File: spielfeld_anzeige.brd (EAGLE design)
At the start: 100 x 60 mm, 19 parts, among them IC1 UDN2981A, IC2 UDN2981A, IC3 74HC595N, IC4 74HC595N, IC5 74HC595N

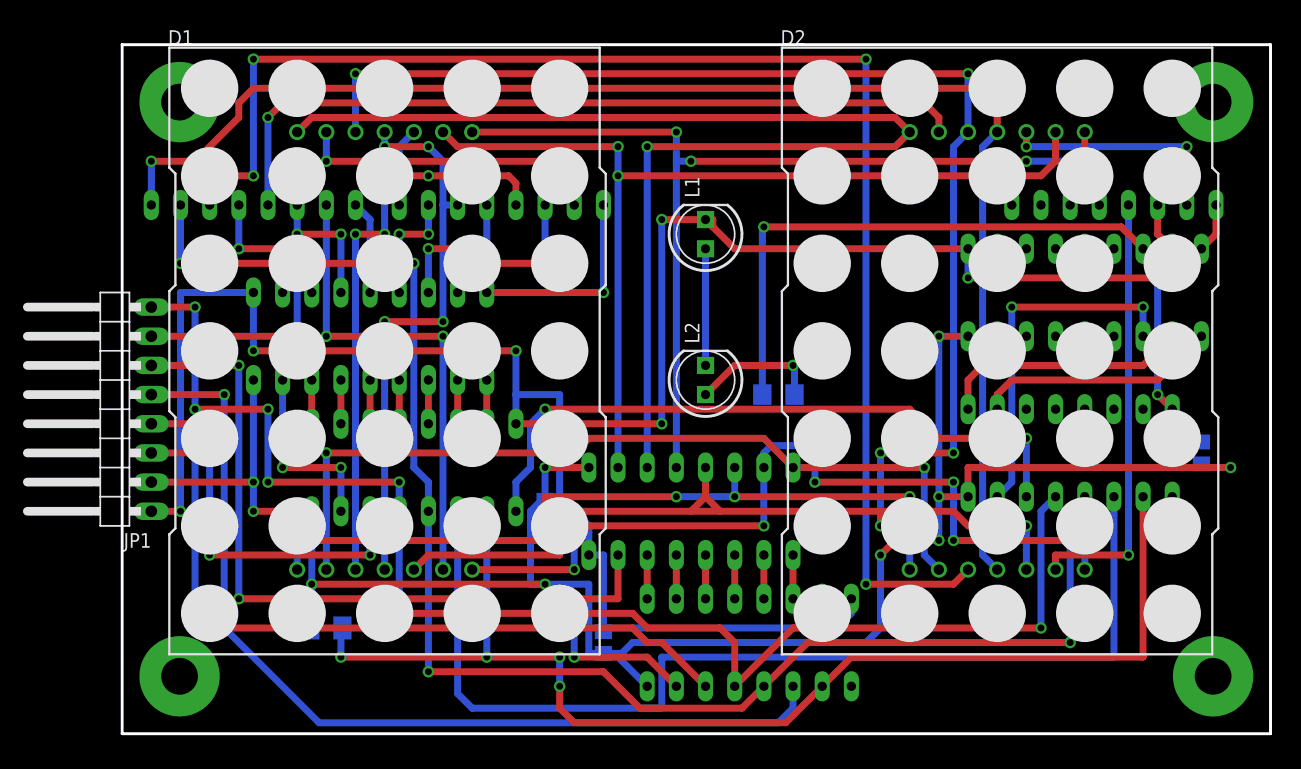
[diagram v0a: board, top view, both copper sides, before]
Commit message: Revision due to Pete and Leander on 30.04.2018
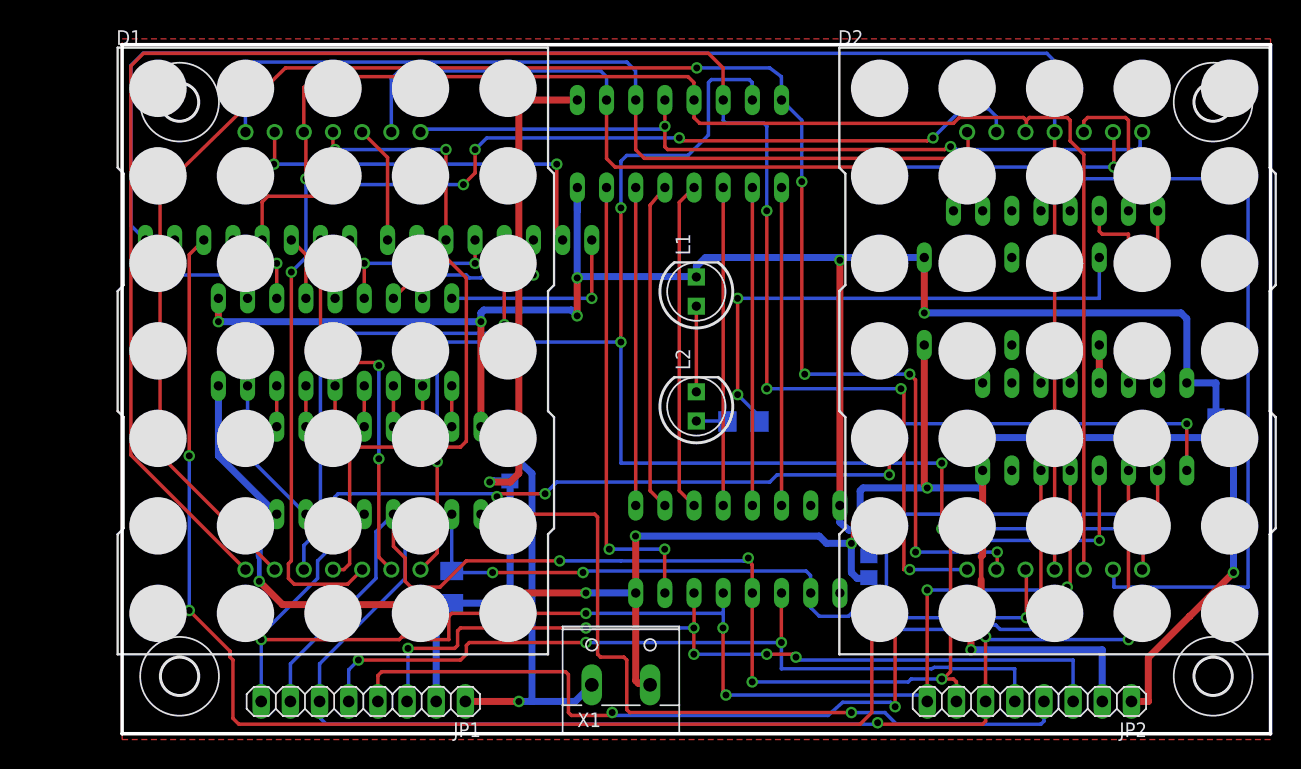
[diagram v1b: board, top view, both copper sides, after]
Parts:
- added H1, H2, H3, H4: MOUNT-HOLE3.2, holes:3,2
- added JP2: OUT, pinhead:1X08
- added X1: (no value), con-wago-508:W237-132
- JP1: value 8 Pin -> IN; device pinhead:1X08/90 -> pinhead:1X08
- RN1, RN2, RN3: value 180 -> 120
- moved JP1 33.8 mm to (21.0, 22.8), turned to 180 degrees
- moved ICL1 32.0 mm to (48.5, 71.4)
- moved C1 24.0 mm to (65.0, 34.5)
- moved R3 11.5 mm to (28.7, 32.8), turned to 270 degrees
- moved IC3 8.19 mm to (53.6, 36.1)
- moved RN3 5.11 mm to (81.3, 65.5)
- moved L1 5.06 mm to (50.0, 58.5)
- moved D2 5.00 mm to (81.2, 53.3)
- moved C2 4.72 mm to (33.8, 43.0), turned to 90 degrees
- moved D1 4.50 mm to (18.4, 53.3)
- moved IC2 3.89 mm to (80.0, 57.7)
- moved R1 3.84 mm to (54.1, 47.2), turned to 180 degrees
- moved RN1 3.21 mm to (32.0, 63.0)
- moved RN2 3.09 mm to (10.9, 63.0)
- moved IC1 3.09 mm to (18.5, 54.1)
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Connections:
- new net COL_SER_OUT: IC4.9, JP2.4
- net !ENABLE!: now also JP2.8
- net +5V: now also JP2.2, X1.2
- net COLON: now also IC5.5; no longer IC5.15
- net COL_SCK: now also JP2.6
- net COL_SER: now also IC5.14; no longer IC4.14
- net D2_C4: now also IC5.7; no longer IC5.2
- net D2_C5: now also IC5.6; no longer IC5.1
- net GND: now also JP2.1, X1.1
- net N$20: now also IC4.14, IC5.9; no longer IC4.9, IC5.14
- net RCK: now also JP2.7
- net ROW_SCK: now also JP2.5
- net ROW_SER: now also JP2.3
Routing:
- net R5_OUT: track 68.6 -> 165.0 mm
- net R7_OUT: track 73.2 -> 156.1 mm, vias 2 -> 6
- net COL_SER_OUT: track 0.00 -> 68.0 mm, vias 0 -> 1
- net R6_OUT: track 73.4 -> 136.1 mm, vias 7 -> 6
- net +5V: track 175.8 -> 236.4 mm
- net COL_SER: track 34.3 -> 85.0 mm, vias 3 -> 4
- net D2_C5_OUT: track 38.1 -> 67.1 mm
- net COLON: track 31.0 -> 3.30 mm, vias 2 -> 0
- net R2_OUT: track 105.7 -> 78.3 mm, vias 1 -> 0
- net N$20: track 58.0 -> 85.2 mm, vias 2 -> 5
- net N$11: track 3.81 -> 28.8 mm
- net N$10: track 3.81 -> 28.7 mm
- net !SCLR!: track 106.5 -> 81.9 mm, vias 4 -> 3
- net COL_SCK: track 139.0 -> 115.1 mm
- net N$9: track 3.81 -> 27.7 mm
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- added copper zone on layer 1, net GND

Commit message: Changed Layout (in Progress)
Updated Eagle-Borad and Schematic
- Reorganize the outputs of the FFs
- Move Colon to FF for Rows
- Change resistors to 0805 and 82 Ohm
- Put all devices in Layout back to 50 mil grid
- startet layout from scratch
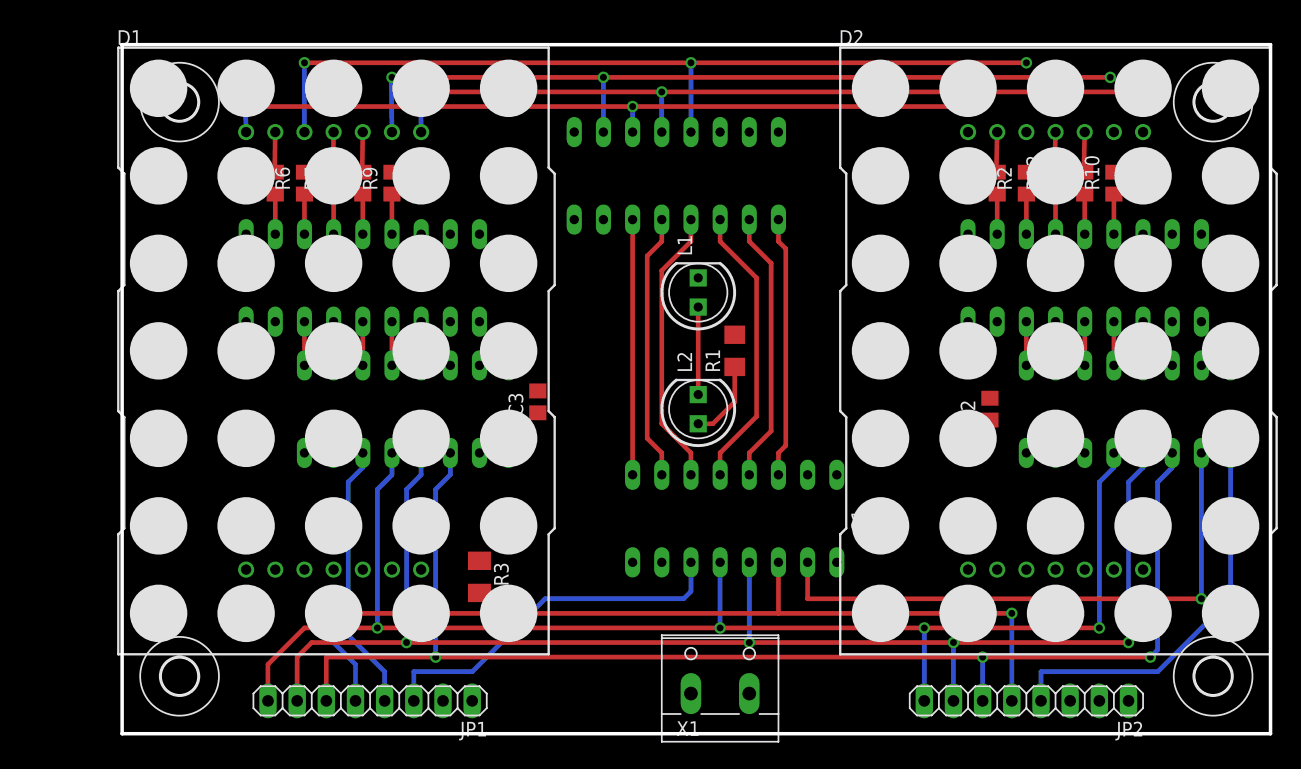
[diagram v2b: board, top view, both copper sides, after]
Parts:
- removed RN1, RN2, RN3: 120, resistor-sil:SIL8
- added R10, R11, R12, R2, R4, R5, R6, R7, R8, R9: 82, rcl:R0805
- moved IC1 65.5 mm to (83.8, 59.7)
- moved IC4 65.5 mm to (87.6, 48.3)
- moved C3 59.1 mm to (36.2, 48.9), flipped to the top
- moved IC2 59.1 mm to (21.0, 59.7)
- moved IC5 59.1 mm to (24.8, 48.3)
- moved C2 42.1 mm to (75.6, 48.3), flipped to the top
- moved X1 8.67 mm to (52.1, 24.1)
- moved R1 6.20 mm to (53.3, 53.3), flipped to the top, turned to 90 degrees
- moved C1 4.31 mm to (66.0, 38.7), flipped to the top
- moved ICL1 2.80 mm to (48.3, 68.6)
- moved IC3 2.68 mm to (53.3, 38.7)
- moved R3 2.57 mm to (31.1, 33.7), flipped to the top
- moved JP1 0.59 mm to (21.6, 22.9)
- moved L2 0.29 mm to (50.2, 48.3)
- moved JP2 0.26 mm to (78.7, 22.9)
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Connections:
- net COLON: now also IC2.1, IC3.7; no longer IC2.3, IC5.5
- net COLON_OUT: now also IC2.18; no longer IC2.16
- net D1_C1: now also IC2.8, IC5.15; no longer IC1.1, IC4.7
- net D1_C1_OUT: now also R5.2; no longer RN1.2
- net D1_C2: now also IC2.7, IC5.1; no longer IC1.2, IC4.6
- net D1_C2_OUT: now also R6.2; no longer RN1.4
- net D1_C3: now also IC2.6, IC5.2; no longer IC1.3, IC4.5
- net D1_C3_OUT: now also R7.2; no longer D1.4, RN1.6
- net D1_C4: now also IC2.5, IC5.3; no longer IC1.4, IC4.4
- net D1_C4_OUT: now also R8.2; no longer RN1.8
- net D1_C5: now also IC2.4, IC5.4; no longer IC1.5, IC4.3
- net D1_C5_OUT: now also R9.2; no longer RN2.2
- net D2_C1: now also IC1.8, IC4.15; no longer IC1.6, IC4.2
- net D2_C1_OUT: now also R4.2; no longer RN2.4
- net D2_C2_OUT: now also R2.2; no longer RN2.6
- net D2_C3: now also IC1.6, IC4.2; no longer IC1.8, IC4.15
- net D2_C3_OUT: now also R12.2; no longer D2.4, RN2.8
- net D2_C4: now also IC1.5, IC4.3; no longer IC2.1, IC5.7
- net D2_C4_OUT: now also R11.2; no longer RN3.2
- net D2_C5: now also IC1.4, IC4.4; no longer IC2.2, IC5.6
- net D2_C5_OUT: now also R10.2; no longer RN3.4
- net N$14: now also R11.1; no longer RN2.1
- net N$15: now also R12.1; no longer RN2.3
- net N$16: now also R2.1; no longer RN2.5
- net N$17: now also R4.1; no longer RN2.7
- net N$2: now also IC2.11, R5.1; no longer IC1.18, RN1.1
- net N$3: now also IC2.12, R6.1; no longer IC1.17, RN1.3
- net N$4: now also IC2.13, R7.1; no longer IC1.16, RN1.5
- net N$5: now also IC2.14, R8.1; no longer IC1.15, RN1.7
- net N$6: now also IC2.15, R9.1; no longer IC2.18, RN3.1
- net N$7: now also IC1.15, R10.1; no longer IC2.17, RN3.3
- net R4_OUT: no longer D1.5, D2.5
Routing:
- net +5V: track 236.4 -> 0.00 mm, vias 10 -> 0
- net GND: track 224.7 -> 0.00 mm, vias 8 -> 0
- net R5_OUT: track 165.0 -> 0.00 mm, vias 4 -> 0
- net R7_OUT: track 156.1 -> 0.00 mm, vias 6 -> 0
- net D2_C3_OUT: track 141.2 -> 3.58 mm
- net R6_OUT: track 136.1 -> 0.00 mm, vias 6 -> 0
- net D2_C2_OUT: track 125.7 -> 0.00 mm, vias 4 -> 0
- net R4_OUT: track 162.5 -> 74.9 mm, vias 2 -> 3
- net N$20: track 85.2 -> 0.00 mm, vias 5 -> 0
- net D2_C1_OUT: track 73.6 -> 3.58 mm, vias 5 -> 0
- net D2_C5_OUT: track 67.1 -> 0.00 mm, vias 1 -> 0
- net COL_SER: track 85.0 -> 23.4 mm, vias 4 -> 0
- net D1_C3_OUT: track 59.3 -> 3.55 mm, vias 2 -> 0
- net COLON_OUT: track 46.6 -> 0.00 mm, vias 2 -> 0
- net D1_C2_OUT: track 44.6 -> 0.00 mm, vias 1 -> 0
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- removed copper zone on layer 1, net GND
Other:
- board text added: "ToDo: - Power Nets - Kennzeichnung +/- an Power Connector - Kennzeichnung In/Out Connector Data - GND/VDD Plane?"

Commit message: Layout fertig
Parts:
- moved C3 6.98 mm to (36.2, 55.9), turned to 270 degrees
- moved C1 6.35 mm to (71.1, 42.5), turned to 180 degrees
- moved R1 5.40 mm to (47.9, 53.3), flipped to the bottom
- moved C2 4.26 mm to (73.7, 52.1), turned to 270 degrees
- moved R3 2.84 mm to (33.7, 34.9), turned to 0 degrees
- moved R2 0.95 mm to (77.8, 67.9)
- moved R4 0.95 mm to (75.2, 67.9)
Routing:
- net +5V: track 0.00 -> 306.7 mm, vias 0 -> 7
- net GND: track 0.00 -> 256.6 mm, vias 0 -> 4
- net R5_OUT: track 0.00 -> 110.8 mm, vias 0 -> 3
- net R6_OUT: track 0.00 -> 109.0 mm, vias 0 -> 3
- net R7_OUT: track 0.00 -> 107.2 mm
- net D1_C5_OUT: track 0.00 -> 80.8 mm, vias 0 -> 2
- net N$20: track 0.00 -> 55.9 mm, vias 0 -> 2
- net D1_C2_OUT: track 0.00 -> 53.8 mm, vias 0 -> 2
- net ROW_SER: track 32.1 -> 74.0 mm, vias 0 -> 3
- net D2_C2_OUT: track 0.00 -> 39.1 mm, vias 0 -> 1
- net !SCLR!: track 50.2 -> 89.2 mm
- net COLON: track 0.00 -> 38.2 mm, vias 0 -> 1
- net D2_C5_OUT: track 0.00 -> 36.9 mm, vias 0 -> 1
- net N$8: track 0.00 -> 33.0 mm, vias 0 -> 1
- net COLON_OUT: track 0.00 -> 22.1 mm, vias 0 -> 1
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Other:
- board text added: "+"
- board text added: "-"
- board text added: "5V"
- board text added: "IN"
- board text added: "OUT"
- board text added: "ROBOSAX 2018"
- board text removed: "ToDo: - Power Nets - Kennzeichnung +/- an Power Connector - Kennzeichnung In/Out Connector Data - GND/VDD Plane?"

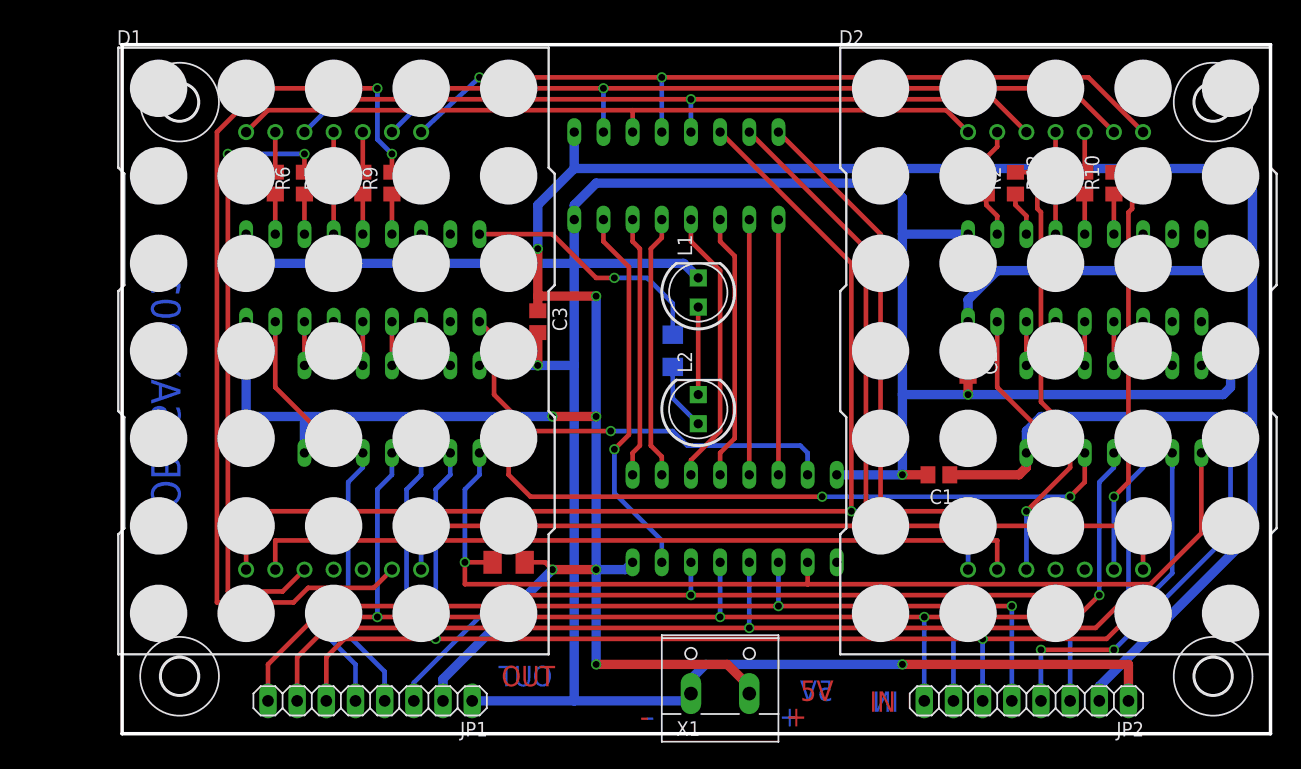
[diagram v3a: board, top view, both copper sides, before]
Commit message: Korrekturen Layout
LEDs ins mm-Raster zurückgesetzt.
Maßangaben korrigiert.
Die freien Eingänge der Treiber-ICs mit GND verbunden.
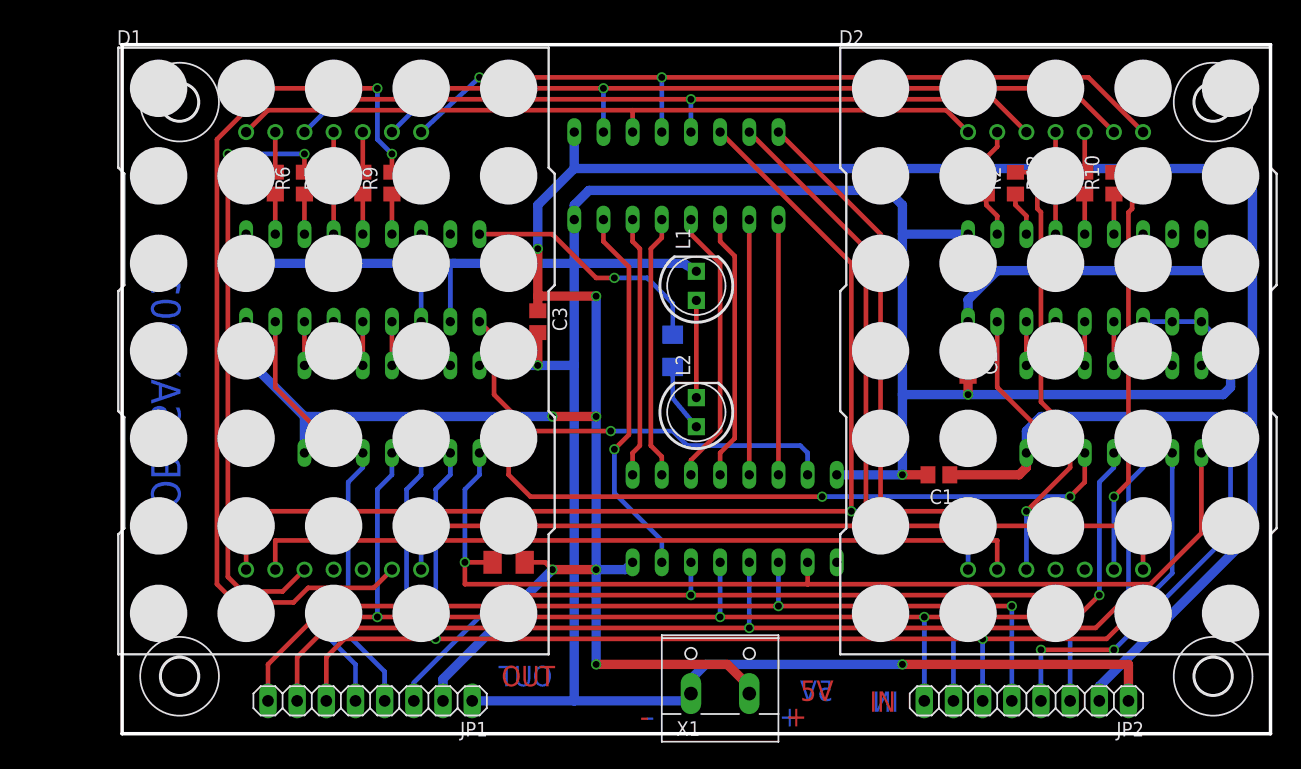
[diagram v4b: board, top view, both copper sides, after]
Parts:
- moved L1 0.60 mm to (50.0, 59.0)
- moved L2 0.31 mm to (50.0, 48.0)
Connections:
- net GND: now also IC1.1, IC1.2, IC1.3, IC2.2, IC2.3
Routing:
- net GND: track 256.6 -> 276.2 mm
- net +5V: track 306.7 -> 303.7 mm
- net D1_C5_OUT: track 80.8 -> 79.5 mm
- net N$1: track 7.62 -> 8.46 mm
- net D1_C2_OUT: track 53.8 -> 53.1 mm
